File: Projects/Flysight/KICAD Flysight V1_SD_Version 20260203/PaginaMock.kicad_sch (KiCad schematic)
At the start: 2 parts, among them Y4 TSX-322524.0000MF15X-AC3

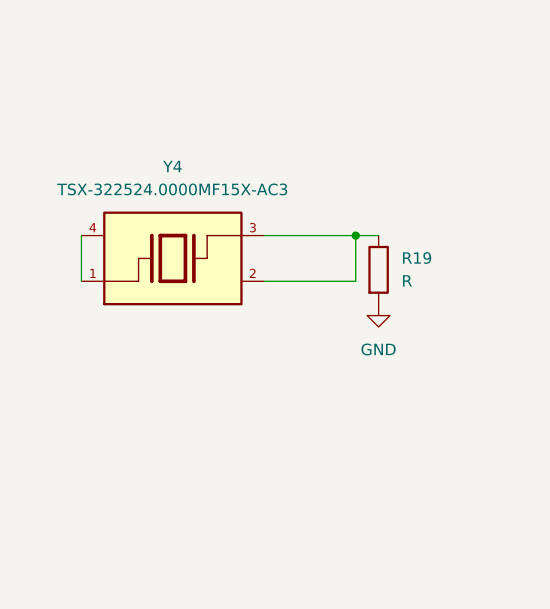
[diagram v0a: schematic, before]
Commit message: another Oscilator (Y4) was added to the project
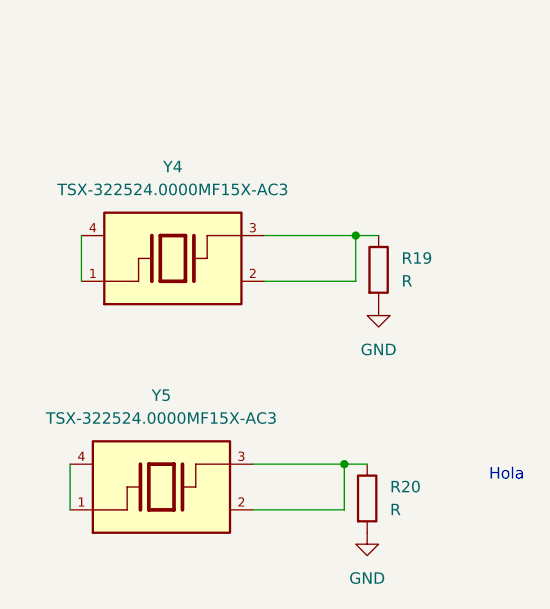
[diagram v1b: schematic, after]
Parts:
- added R20: R, symbol Device:R
- added Y5: TSX-322524.0000MF15X-AC3, oscilator:4SMD, symbol Osc:TSX-322524.0000MF15X-AC3
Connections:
- net GND: now also R20.2
- new net: Y5.1, Y5.4
- new net: R20.1, Y5.2, Y5.3
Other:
- note added: "Hola"

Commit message: added capacitor
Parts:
- added C20: GRM155C80J225KE95D, GRM155C80J225KE95D:CAPC1005X55N, symbol Test2:GRM155C80J225KE95D
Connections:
- new net +1V0: C20.2
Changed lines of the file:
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@@
+	)
+	(symbol
+		(lib_id "power:+1V0")
+		(at 149.86 59.69 0)
+		(unit 1)
+		(exclude_from_sim no)
+		(in_bom yes)
+		(on_board yes)
+		(dnp no)
+		(fields_autoplaced yes)
+		(property "Reference" "#PWR096"
+			(at 149.86 63.5 0)
+			(effects
+				(font
+					(size 1.27 1.27)
+				)
+				(hide yes)
+			)
+		)
+		(property "Value" "+1V0"
+			(at 149.86 54.61 0)
+			(effects
+				(font
+					(size 1.27 1.27)
+				)
+			)
+		)
+		(property "Footprint" ""
+			(at 149.86 59.69 0)
+			(effects
+				(font
+					(size 1.27 1.27)
+				)
+				(hide yes)
+			)
+		)
+		(property "Datasheet" ""
+			(at 149.86 59.69 0)
+			(effects
+				(font
+					(size 1.27 1.27)
+				)
+				(hide yes)
+			)
+		)
+		(property "Description" "Power symbol creates a global label with name \"+1V0\""
+			(at 149.86 59.69 0)
+			(effects
+				(font
+					(size 1.27 1.27)
+				)
+				(hide yes)
+			)
+		)
+		(pin "1"
+		)
+		(instances
+			(project ""
+				(path "/0650c7a8-acba-429c-9f8e-eec0baf0bc1c/fede4c36-00cc-4d3d-b71c-5243ba232202/7c25b967-6a62-4506-be6e-79fa429d9459"
+					(reference "#PWR096")
+					(unit 1)
+				)
+			)
+		)
+	)
+	(symbol
+		(lib_id "Test2:GRM155C80J225KE95D")
+		(at 144.78 59.69 0)
+		(unit 1)
+		(exclude_from_sim no)
+		(in_bom yes)
+		(on_board yes)
+		(dnp no)
+		(fields_autoplaced yes)
+		(property "Reference" "C20"
+			(at 146.05 53.34 0)
+			(effects
+				(font
+					(size 1.27 1.27)
+				)
+			)
+		)
+		(property "Value" "GRM155C80J225KE95D"
+			(at 146.05 55.88 0)
+			(effects
+				(font
+					(size 1.27 1.27)
+				)
+			)
+		)
+		(property "Footprint" "GRM155C80J225KE95D:CAPC1005X55N"
+			(at 144.78 59.69 0)
+			(effects
+				(font
+					(size 1.27 1.27)
+				)
+				(justify bottom)
+				(hide yes)
+			)
+		)
+		(property "Datasheet" ""
+			(at 144.78 59.69 0)
+			(effects
+				(font
+					(size 1.27 1.27)
+				)
+				(hide yes)
+			)
+		)
+		(property "Description" ""
+			(at 144.78 59.69 0)
+			(effects
+				(font
+					(size 1.27 1.27)
+				)
+				(hide yes)
+			)
+		)
+		(pin "1"
+		)
+		(pin "2"
+		)
+		(instances
+			(project ""
+				(path "/0650c7a8-acba-429c-9f8e-eec0baf0bc1c/fede4c36-00cc-4d3d-b71c-5243ba232202/7c25b967-6a62-4506-be6e-79fa429d9459"
+					(reference "C20")
+					(unit 1)
+				)
+			)
+		)
 	)
 	(symbol
